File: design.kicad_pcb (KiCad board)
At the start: 2 copper layers, 38 x 12 mm, 1 part, among them U1 TPS61099YFFT

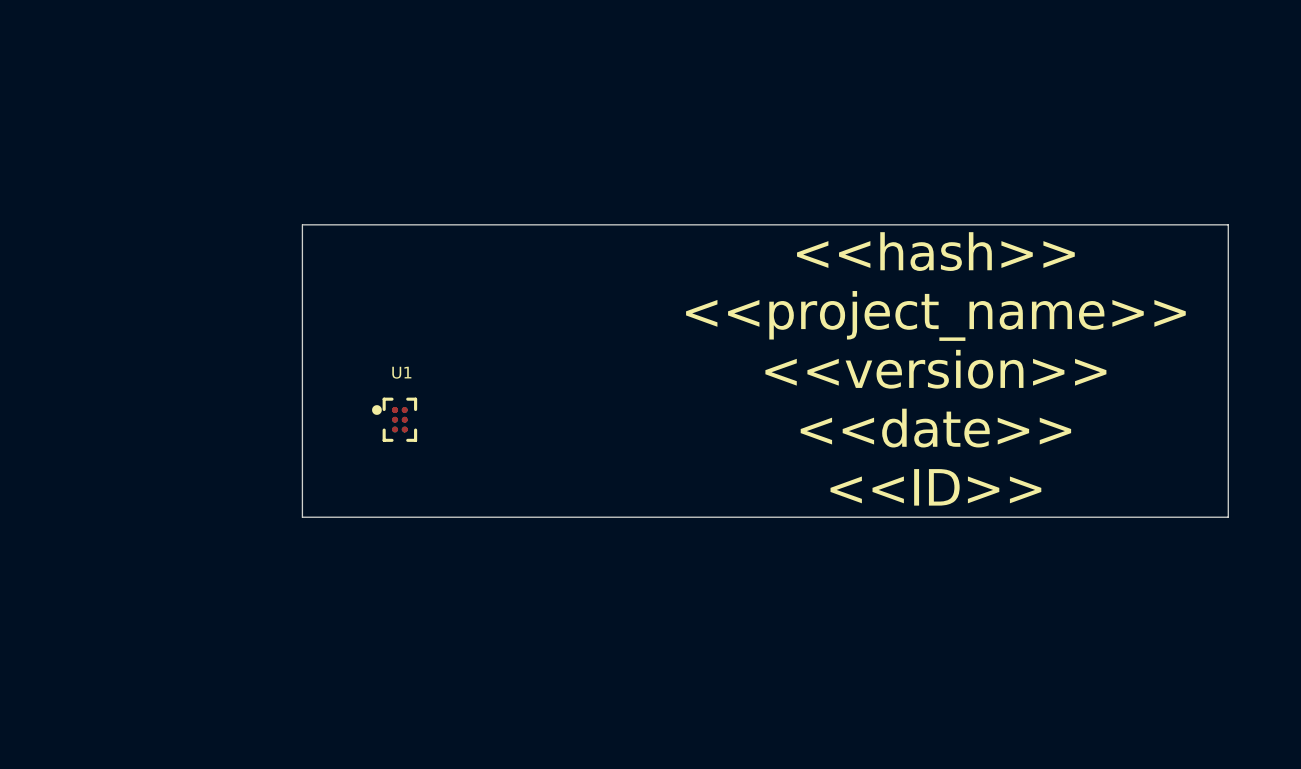
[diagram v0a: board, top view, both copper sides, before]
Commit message: SCH/PCB Add initial design
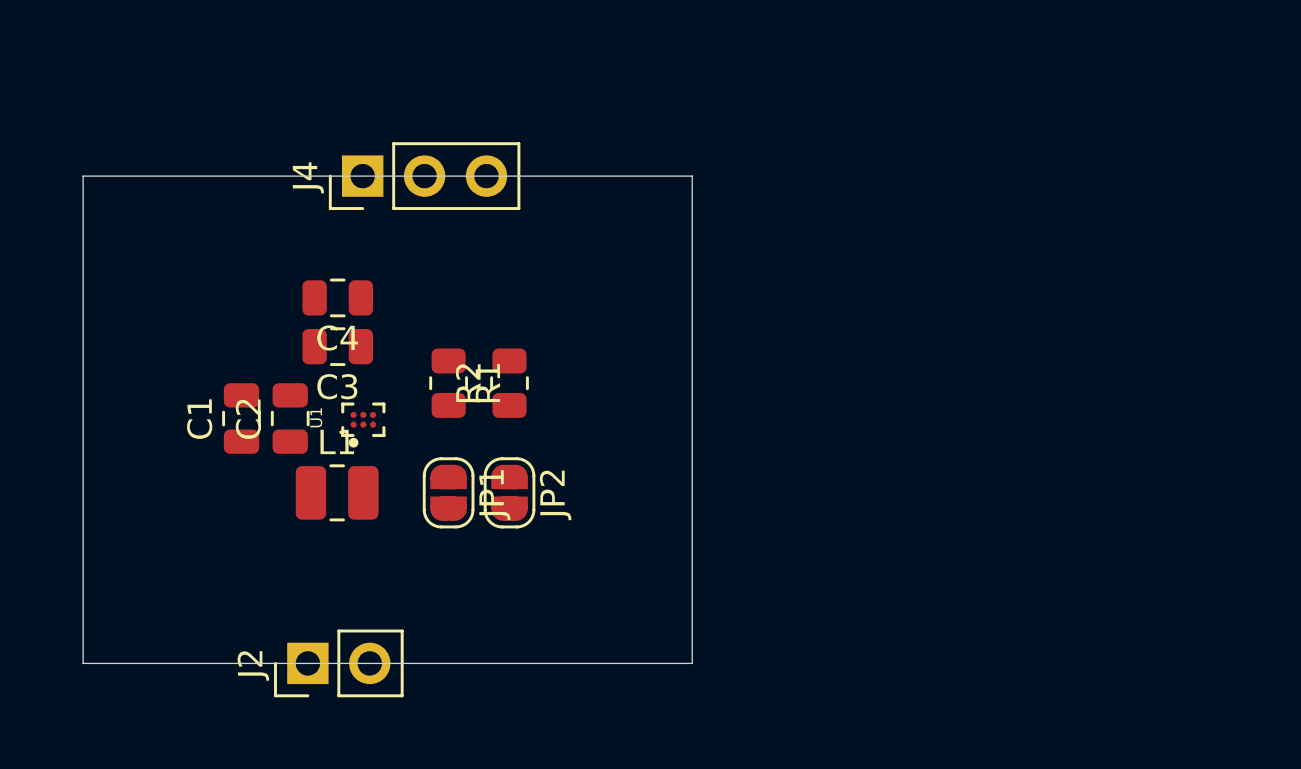
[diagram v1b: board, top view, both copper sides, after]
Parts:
- added C1: C_Small, Capacitor_SMD:C_0805_2012Metric, F.Cu at (140.5, 96.0)
- added C2: C_Small, Capacitor_SMD:C_0805_2012Metric, F.Cu at (142.5, 96.0)
- added C3: C_Small, Capacitor_SMD:C_0805_2012Metric, F.Cu at (144.4, 93.0)
- added C4: C_Small, Capacitor_SMD:C_0805_2012Metric, F.Cu at (144.4, 91.0)
- added J2: Conn_01x02, Connector_PinHeader_2.54mm:PinHeader_1x02_P2.54mm_Vertical, F.Cu at (143.2, 106.0)
- added J4: Conn_01x03, Connector_PinHeader_2.54mm:PinHeader_1x03_P2.54mm_Vertical, F.Cu at (145.5, 86.0)
- added JP1: SolderJumper_2_Open, Jumper:SolderJumper-2_P1.3mm_Open_RoundedPad1.0x1.5mm, F.Cu at (149.0, 99.0)
- added JP2: SolderJumper_2_Open, Jumper:SolderJumper-2_P1.3mm_Open_RoundedPad1.0x1.5mm, F.Cu at (151.5, 99.0)
- added L1: L_Small, Inductor_SMD:L_1008_2520Metric, F.Cu at (144.4, 99.0)
- added R1: R_Small, Resistor_SMD:R_0805_2012Metric, F.Cu at (149.0, 94.5)
- added R2: R_Small, Resistor_SMD:R_0805_2012Metric, F.Cu at (151.5, 94.5)
- moved U1 1.50 mm to (145.5, 96.0), turned to 90 degrees
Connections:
- U1 pad A1: unconnected-(U1-PadA1) -> Vin
- U1 pad A2: unconnected-(U1-PadA2) -> GND
- U1 pad B1: unconnected-(U1-PadB1) -> Net-(L1-Pad2)
- U1 pad B2: unconnected-(U1-PadB2) -> Vout
- U1 pad C1: unconnected-(U1-PadC1) -> En
- U1 pad C2: unconnected-(U1-PadC2) -> FB
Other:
- board size 38 x 12 mm -> 25 x 20 mm

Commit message: SCH/PCB desin according Datasheet
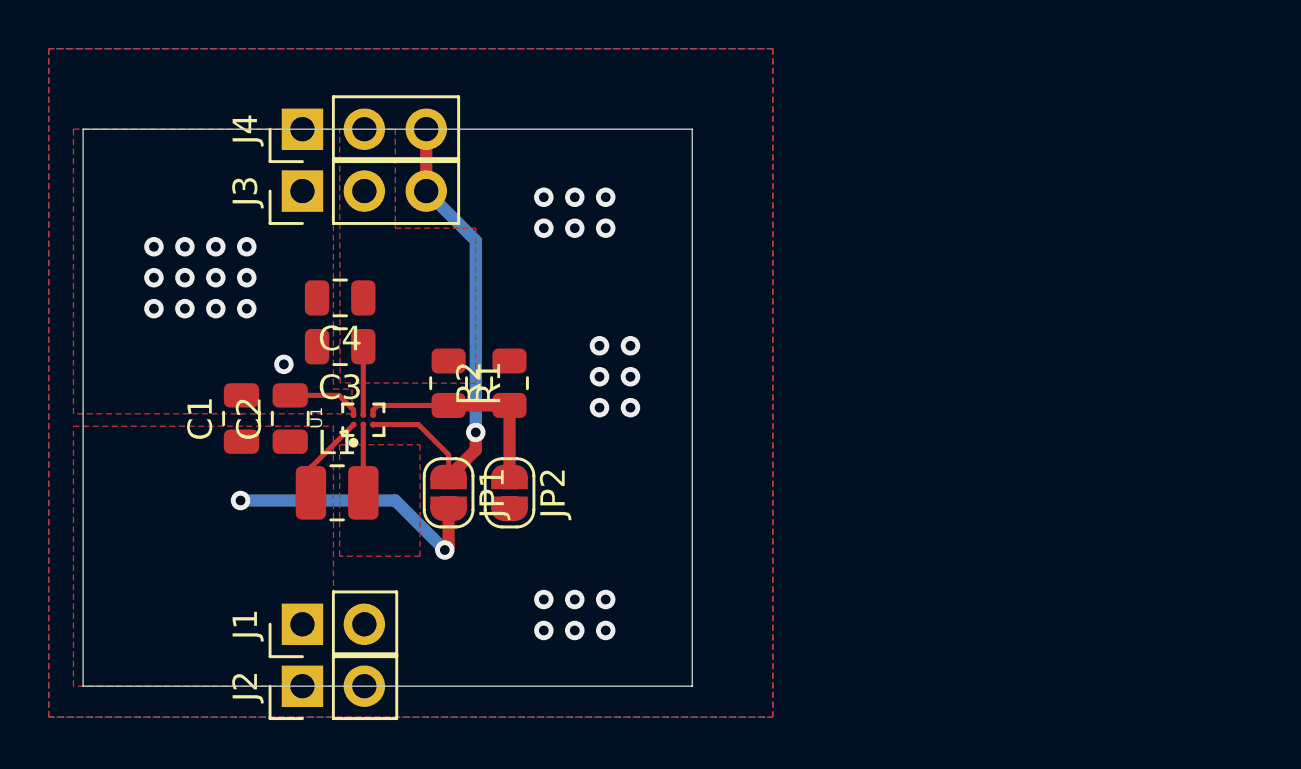
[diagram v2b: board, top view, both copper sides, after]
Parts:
- added J1: Conn_01x02, Connector_PinHeader_2.54mm:PinHeader_1x02_P2.54mm_Vertical, F.Cu at (143.0, 104.4)
- added J3: Conn_01x03, Connector_PinHeader_2.54mm:PinHeader_1x03_P2.54mm_Vertical, F.Cu at (143.0, 86.6)
- moved J4 3.13 mm to (143.0, 84.1)
- moved J2 0.96 mm to (143.0, 106.9)
- moved C3 0.10 mm to (144.6, 93.0)
- moved C4 0.10 mm to (144.6, 91.0)
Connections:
- net Net-(L1-Pad2) renamed SW
- J4 pad 1: Vout -> GND
- J4 pad 2: GND -> Vout
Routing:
- net En: track 0.00 -> 19.9 mm, vias 0 -> 1
- net Vin: track 0.00 -> 14.5 mm, vias 0 -> 2
- net FB: track 0.00 -> 8.82 mm
- net GND: track 0.00 -> 3.05 mm, vias 0 -> 31
- net Vout: track 0.00 -> 2.80 mm
- net SW: track 0.00 -> 2.80 mm
- added copper zone on B.Cu, net GND
- added copper zone on F.Cu, net GND
- added copper zone on F.Cu, net SW
- added copper zone on F.Cu, net Vin
- added copper zone on F.Cu, net Vout
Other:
- board size 25 x 20 mm -> 25 x 22.9 mm

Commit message: PCB Move Silkscreen
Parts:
- moved C1 0.10 mm to (140.6, 96.0)
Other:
- board text added: "EN"
- board text added: "GND"
- board text added: "Vin"
- board text added: "Vout"

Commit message: PCB Add Silkscreen information
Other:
- board text added: "<<project_name>> <<ID>> <<version>> <<date>> <<hash>> gll.wf/p/001"
- board text removed: "<<hash>> <<project_name>> <<version>> <<date>> <<ID>>"
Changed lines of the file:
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@@
   )
   (gr_rect (start 134 84.074) (end 159 106.934) (layer "Edge.Cuts") (width 0.05) (fill none))
-  (gr_text "<<hash>>\n<<project_name>>\n<<version>>\n<<date>>\n<<ID>>" (at 146.5 96) (layer "B.SilkS")
-    (effects (font (size 1.5 1.5) (thickness 0.3)) (justify mirror))
+  (gr_text "<<project_name>>\n<<ID>>\n<<version>>\n<<date>>\n<<hash>>\ngll.wf/p/001" (at 146.5 95.504) (layer "B.SilkS")
+    (effects (font (size 1 1) (thickness 0.15)) (justify mirror))
   )
   (gr_text "GND" (at 143 88.3) (layer "F.SilkS")
